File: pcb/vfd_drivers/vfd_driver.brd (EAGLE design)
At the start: 27.9 x 45.7 mm, 5 parts

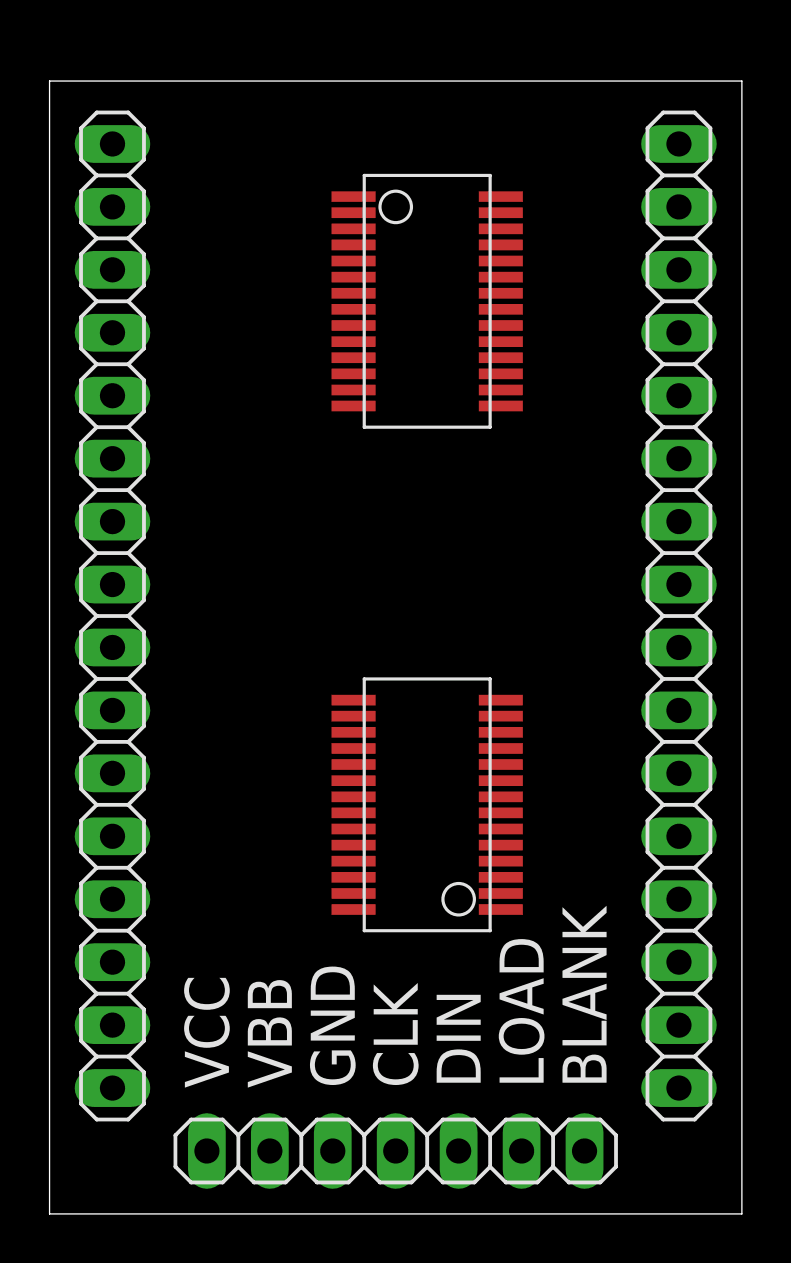
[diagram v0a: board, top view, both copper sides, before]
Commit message: Finalized the VFD driver carrier board
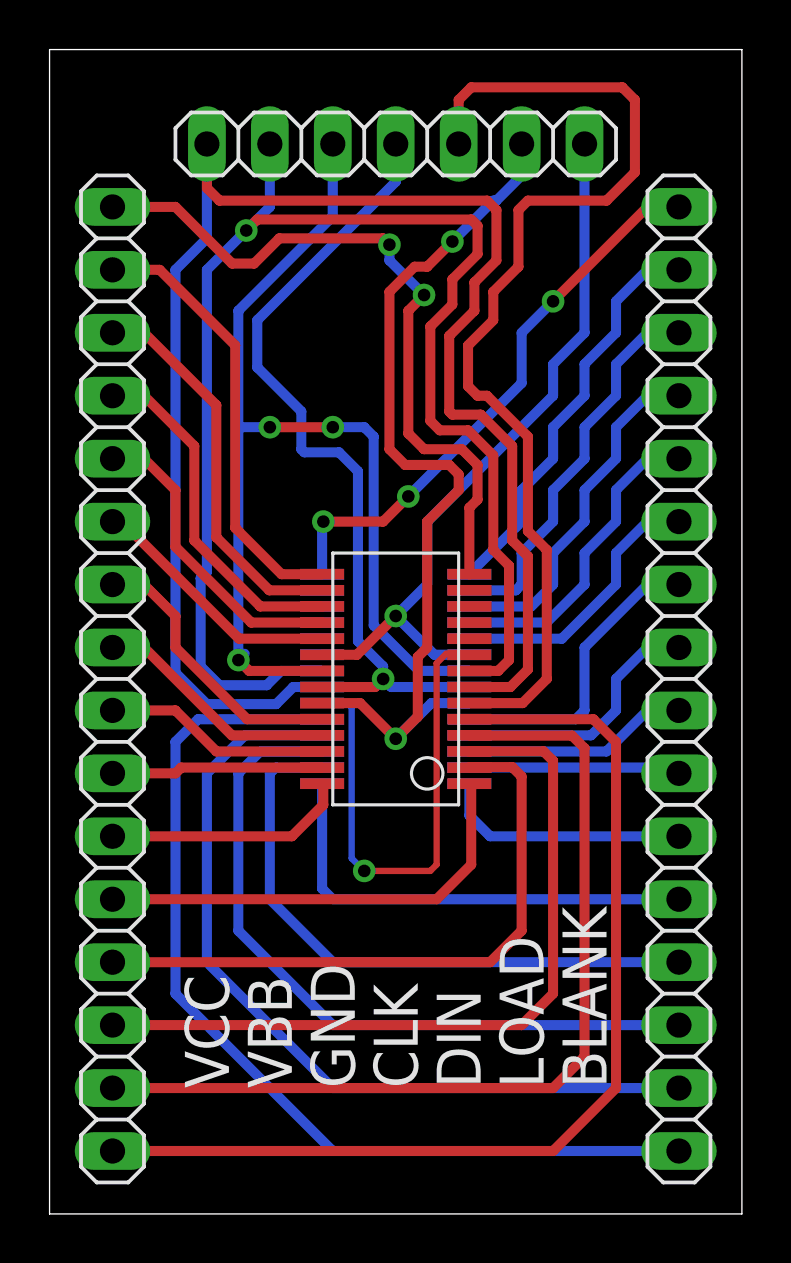
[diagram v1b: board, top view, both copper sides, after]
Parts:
- moved JP3 40.6 mm to (14.0, 43.2), turned to 180 degrees
- moved U$2 15.3 mm to (14.0, 21.6), flipped to the bottom, turned to 270 degrees
- moved U$1 5.24 mm to (14.0, 21.6)
- moved JP1 2.54 mm to (2.54, 21.6)
- moved JP2 2.54 mm to (25.4, 21.6)
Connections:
- removed net N$17: JP2.9, U$2.17
- removed net N$18: JP2.8, U$2.18
- removed net N$19: JP2.7, U$2.19
- removed net N$20: JP2.6, U$2.24
- removed net N$21: JP2.5, U$2.25
- removed net N$22: JP2.4, U$2.26
- removed net N$23: JP2.3, U$2.27
- removed net N$24: JP2.2, U$2.28
- removed net N$25: JP2.1, U$2.1
- new net N$1: JP2.1, U$2.14
- new net N$2: JP2.2, U$2.15
- new net N$3: JP2.3, U$2.16
- new net N$4: JP2.4, U$2.17
- new net N$5: JP2.5, U$2.18
- new net N$6: JP2.6, U$2.19
- new net N$7: JP2.7, U$2.24
- new net N$8: JP2.8, U$2.25
- new net N$9: JP2.9, U$2.26
- net N$10: now also JP2.10, U$2.27; no longer JP2.16, U$2.10
- net N$11: now also JP2.11, U$2.28; no longer JP2.15, U$2.11
- net N$12: now also JP2.12, U$2.1; no longer JP2.14, U$2.12
- net N$13: now also U$2.2; no longer U$2.13
- net N$14: now also JP2.14, U$2.3; no longer JP2.12, U$2.14
- net N$15: now also JP2.15, U$2.4; no longer JP2.11, U$2.15
- net N$16: now also JP2.16, U$2.5; no longer JP2.10, U$2.16
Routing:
- net VCC: track 0.00 -> 66.4 mm
- net VBB: track 0.00 -> 59.4 mm, vias 0 -> 1
- net GND: track 0.00 -> 44.2 mm, vias 0 -> 3
- net DIN: track 0.00 -> 42.4 mm
- net N$48: track 0.00 -> 41.6 mm
- net N$16: track 0.00 -> 39.4 mm
- net LOAD: track 0.00 -> 37.0 mm, vias 0 -> 2
- net N$47: track 0.00 -> 36.9 mm
- net N$15: track 0.00 -> 34.1 mm
- net CLK: track 0.00 -> 33.0 mm, vias 0 -> 1
- net N$46: track 0.00 -> 31.2 mm
- net N$14: track 0.00 -> 29.5 mm
- net BLANK: track 0.00 -> 29.4 mm, vias 0 -> 1
- net N$33: track 0.00 -> 29.0 mm, vias 0 -> 2
- net N$45: track 0.00 -> 25.5 mm
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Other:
- board size 27.9 x 45.7 mm -> 27.9 x 47 mm
